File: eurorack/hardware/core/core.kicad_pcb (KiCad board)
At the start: 2 copper layers, 4 parts, among them J1 Conn, U1 STM32F427VGT6, U2 TLV320AIC23BPW, U3 LM1117F-3.3

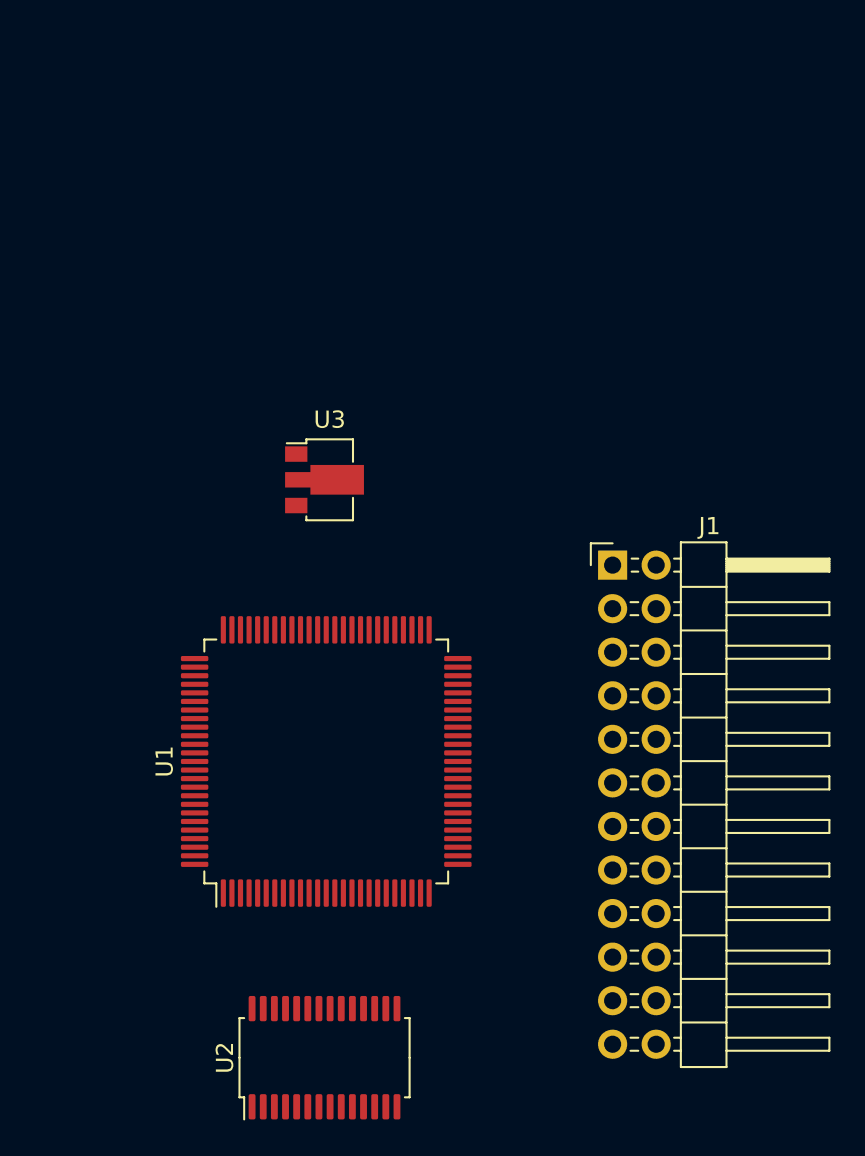
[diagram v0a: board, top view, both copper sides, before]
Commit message: Add connections to eurorack core
Signed-off-by: Petr Horacek <hrck@protonmail.com>
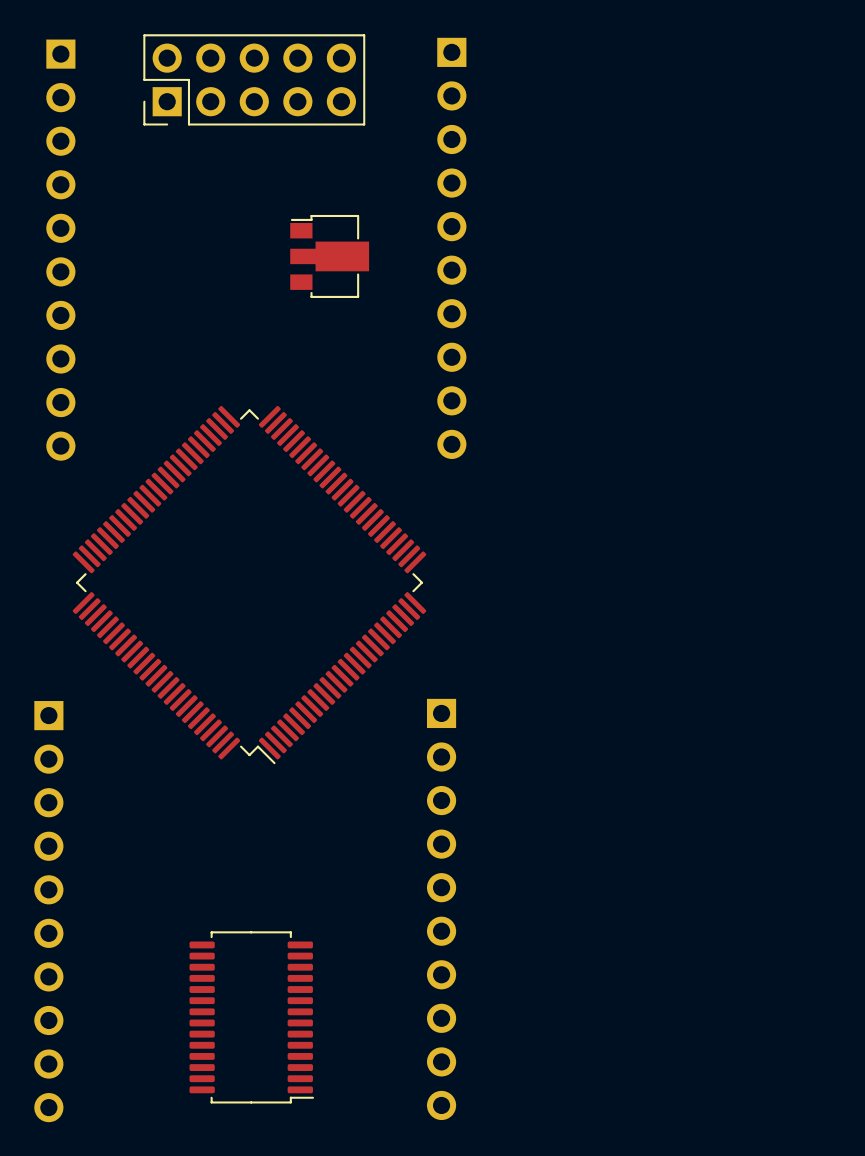
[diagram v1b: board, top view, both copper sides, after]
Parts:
- added J2: ConnSW, Connector_PinHeader_2.54mm:PinHeader_1x10_P2.54mm_Vertical, B.Cu at (111.0, 62.1)
- added J3: ConnNE, Connector_PinHeader_2.54mm:PinHeader_1x10_P2.54mm_Vertical, B.Cu at (134.4, 23.4)
- added J4: ConnSE, Connector_PinHeader_2.54mm:PinHeader_1x10_P2.54mm_Vertical, B.Cu at (133.8, 62.0)
- added J5: Power, Connector_PinHeader_2.54mm:PinHeader_2x05_P2.54mm_Vertical, F.Cu at (117.8, 26.3)
- J1: value Conn -> ConnNW; footprint Connector_PinHeader_2.54mm:PinHeader_2x12_P2.54mm_Horizontal -> Connector_PinHeader_2.54mm:PinHeader_1x10_P2.54mm_Vertical; moved to B.Cu
- moved J1 43.9 mm to (111.7, 23.6), turned to 180 degrees
- moved U3 13.0 mm to (127.3, 35.4)
- moved U1 11.3 mm to (122.7, 54.4), turned to 135 degrees
- moved U2 4.88 mm to (122.8, 79.7), turned to 180 degrees

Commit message: Add basic MCU peripherals and power
Signed-off-by: Petr Horacek <hrck@protonmail.com>
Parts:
- added C1: 20p, Capacitor_SMD:C_0402_1005Metric, F.Cu at (130.2, 65.0)
- added C2: 20p, Capacitor_SMD:C_0402_1005Metric, F.Cu at (129.5, 63.5)
- added C3: 2u2, Capacitor_SMD:C_0603_1608Metric, F.Cu at (127.9, 42.0)
- added C4: 2u2, Capacitor_SMD:C_0603_1608Metric, F.Cu at (127.9, 44.5)
- added J6: SWD, Connector_PinHeader_2.54mm:PinHeader_2x05_P2.54mm_Vertical, F.Cu at (117.8, 84.5)
- added R1: 47, Resistor_SMD:R_0402_1005Metric, F.Cu at (129.0, 65.0)
- added Y1: Crystal, Crystal:Crystal_SMD_5032-2Pin_5.0x3.2mm, F.Cu at (127.1, 68.3)
- moved U2 8.38 mm to (118.2, 72.7)
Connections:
- U1 pad 10: Net-(U1-Pad10) -> GND
- U1 pad 100: Net-(U1-Pad100) -> +3V3
- U1 pad 11: Net-(U1-Pad11) -> +3V3
- U1 pad 12: Net-(U1-Pad12) -> HSE_IN
- U1 pad 13: Net-(U1-Pad13) -> HSE_OUT
- U1 pad 19: Net-(U1-Pad19) -> +3V3
- U1 pad 20: Net-(U1-Pad20) -> GND
- U1 pad 21: Net-(U1-Pad21) -> +3.3VA
- U1 pad 22: Net-(U1-Pad22) -> +3.3VA
- U1 pad 27: Net-(U1-Pad27) -> GND
- U1 pad 28: Net-(U1-Pad28) -> +3V3
- U1 pad 50: Net-(U1-Pad50) -> +3V3
- U1 pad 6: Net-(U1-Pad6) -> +3V3
- U1 pad 74: Net-(U1-Pad74) -> GND
- U1 pad 75: Net-(U1-Pad75) -> +3V3
- U1 pad 99: Net-(U1-Pad99) -> GND

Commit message: Add reset and boot buttons
Signed-off-by: Petr Horacek <hrck@protonmail.com>
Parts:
- added R2: 10k, Resistor_SMD:R_0402_1005Metric, F.Cu at (121.6, 30.7)
- added R3: 10k, Resistor_SMD:R_0402_1005Metric, F.Cu at (124.5, 30.7)
- added SW1: Reset, Button_Switch_SMD:SW_Push_SPST_NO_Alps_SKRK, F.Cu at (130.0, 34.6)
- added SW2: Boot0, Button_Switch_SMD:SW_Push_SPST_NO_Alps_SKRK, F.Cu at (117.0, 34.5)
- moved U3 4.17 mm to (123.2, 36.2)
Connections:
- U1 pad 14: Net-(U1-Pad14) -> NRST
- U1 pad 94: Net-(U1-Pad94) -> BOOT0

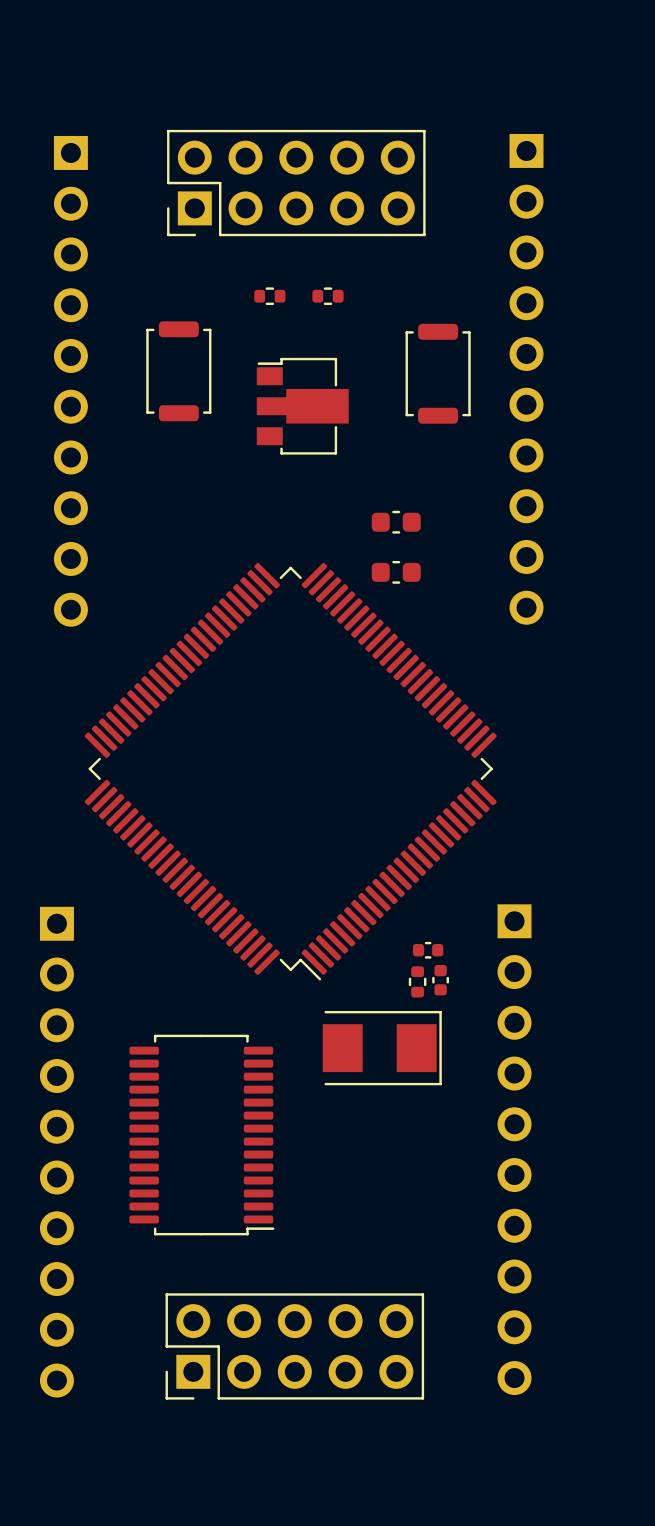
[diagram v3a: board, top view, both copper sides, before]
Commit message: Isoolate 3.3v power from MCU
Signed-off-by: Petr Horacek <hrck@protonmail.com>
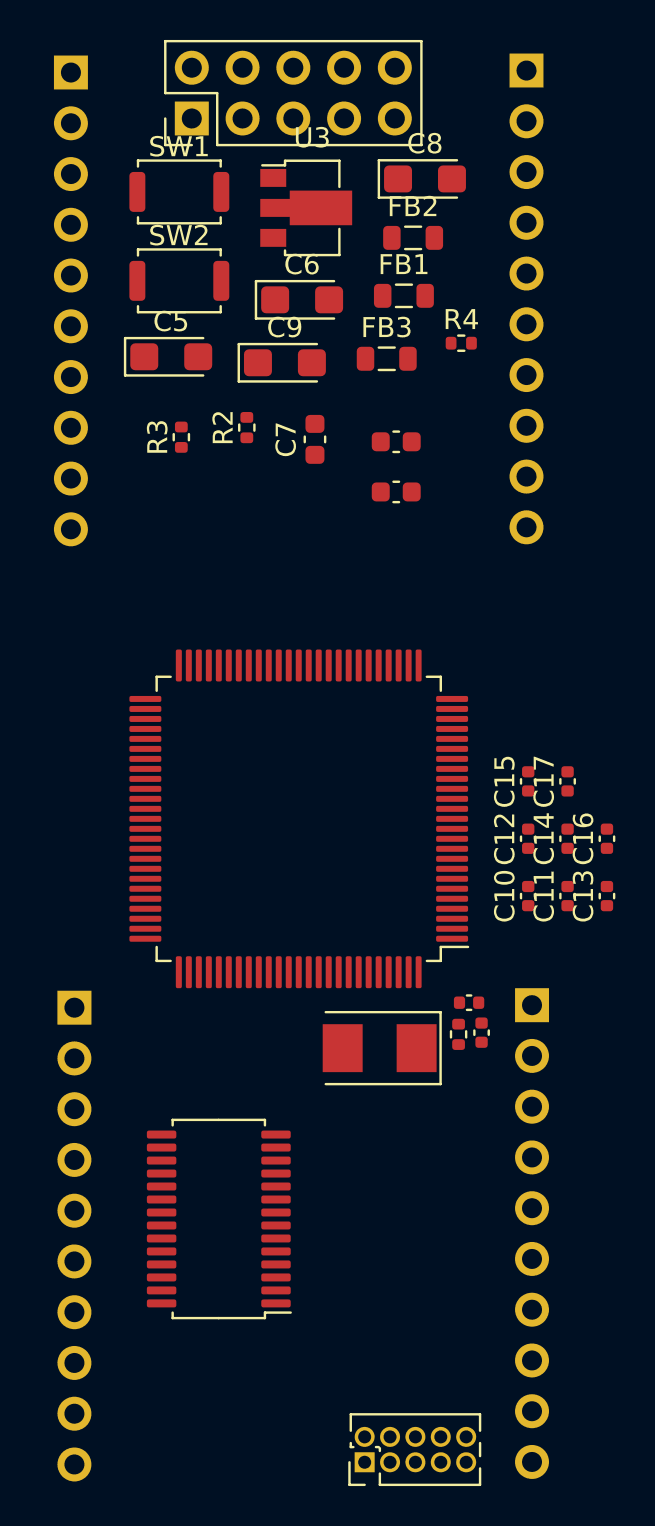
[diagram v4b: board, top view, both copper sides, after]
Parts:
- added C10: 1u, Capacitor_SMD:C_0402_1005Metric, F.Cu at (134.5, 60.7)
- added C11: 100n, Capacitor_SMD:C_0402_1005Metric, F.Cu at (136.5, 60.7)
- added C12: 100n, Capacitor_SMD:C_0402_1005Metric, F.Cu at (134.5, 57.9)
- added C13: 100n, Capacitor_SMD:C_0402_1005Metric, F.Cu at (138.5, 60.7)
- added C14: 100n, Capacitor_SMD:C_0402_1005Metric, F.Cu at (136.5, 57.9)
- added C15: 100n, Capacitor_SMD:C_0402_1005Metric, F.Cu at (134.5, 55.0)
- added C16: 100n, Capacitor_SMD:C_0402_1005Metric, F.Cu at (138.5, 57.9)
- added C17: 100n, Capacitor_SMD:C_0402_1005Metric, F.Cu at (136.5, 55.0)
- added C5: 47u, Capacitor_Tantalum_SMD:CP_EIA-3216-18_Kemet-A, F.Cu at (116.7, 33.8)
- added C6: 47u, Capacitor_Tantalum_SMD:CP_EIA-3216-18_Kemet-A, F.Cu at (123.2, 30.9)
- added C7: 2u2, Capacitor_SMD:C_0603_1608Metric, F.Cu at (123.9, 37.9)
- added C8: 47u, Capacitor_Tantalum_SMD:CP_EIA-3216-18_Kemet-A, F.Cu at (129.4, 24.9)
- added C9: 47u, Capacitor_Tantalum_SMD:CP_EIA-3216-18_Kemet-A, F.Cu at (122.4, 34.1)
- added FB1: Ferrite_Bead_Small, Inductor_SMD:L_0805_2012Metric, F.Cu at (128.3, 30.7)
- added FB2: Ferrite_Bead_Small, Inductor_SMD:L_0805_2012Metric, F.Cu at (128.8, 27.8)
- added FB3: Ferrite_Bead_Small, Inductor_SMD:L_0805_2012Metric, F.Cu at (127.5, 33.9)
- added R4: 15, Resistor_SMD:R_0402_1005Metric, F.Cu at (131.2, 33.1)
- J6: footprint Connector_PinHeader_2.54mm:PinHeader_2x05_P2.54mm_Vertical -> Connector_PinHeader_1.27mm:PinHeader_2x05_P1.27mm_Vertical
- moved SW1 15.8 mm to (117.1, 25.5), turned to 0 degrees
- moved R3 10.2 mm to (117.2, 37.8), turned to 90 degrees
- moved U3 9.93 mm to (123.4, 26.3)
- moved J6 9.70 mm to (126.3, 89.1)
- moved R2 6.67 mm to (120.5, 37.3), turned to 90 degrees
- moved SW2 4.53 mm to (117.1, 30.0), turned to 0 degrees
- moved J5 4.50 mm to (117.7, 21.8)
- moved J2 4.29 mm to (111.8, 66.3)
- moved J4 4.29 mm to (134.7, 66.2)
- moved U2 4.29 mm to (119.0, 76.9)
- moved J1 4.03 mm to (111.7, 19.5)
- moved C3 4.02 mm to (127.9, 38.0)
- moved C4 4.02 mm to (127.9, 40.5)
- moved J3 4.02 mm to (134.4, 19.4)
- moved R1 3.33 mm to (131.1, 67.7)
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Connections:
- J5 pad 1: Net-(J5-Pad1) -> Net-(FB1-Pad1)
- J5 pad 10: Net-(J5-Pad10) -> Net-(FB2-Pad1)
- J5 pad 2: Net-(J5-Pad2) -> Net-(FB1-Pad1)
- J5 pad 3: Net-(J5-Pad3) -> GND
- J5 pad 4: Net-(J5-Pad4) -> GND
- J5 pad 5: Net-(J5-Pad5) -> GND
- J5 pad 6: Net-(J5-Pad6) -> GND
- J5 pad 7: Net-(J5-Pad7) -> GND
- J5 pad 8: Net-(J5-Pad8) -> GND
- J5 pad 9: Net-(J5-Pad9) -> Net-(FB2-Pad1)
- U3 pad 1: Net-(U3-Pad1) -> GND
- U3 pad 2: Net-(U3-Pad2) -> +3V3

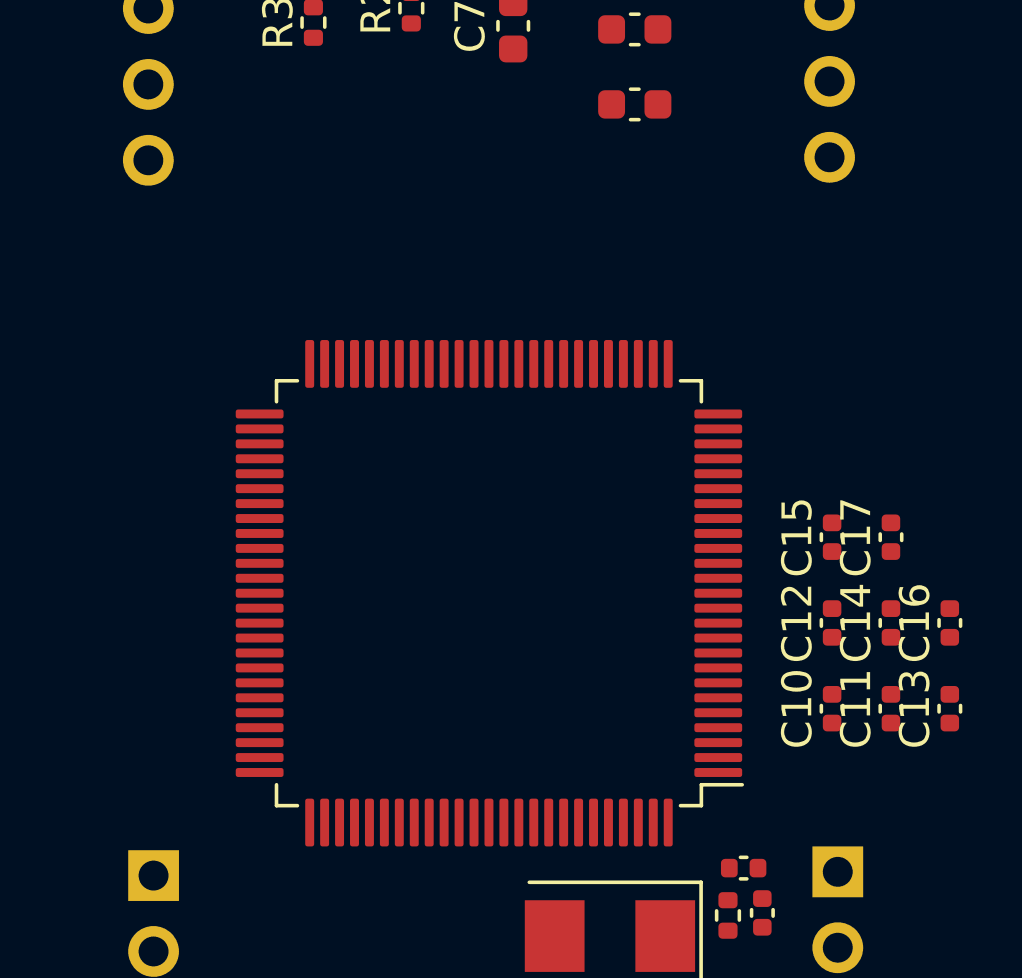
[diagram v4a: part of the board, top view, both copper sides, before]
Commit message: Add decoupling capacitors
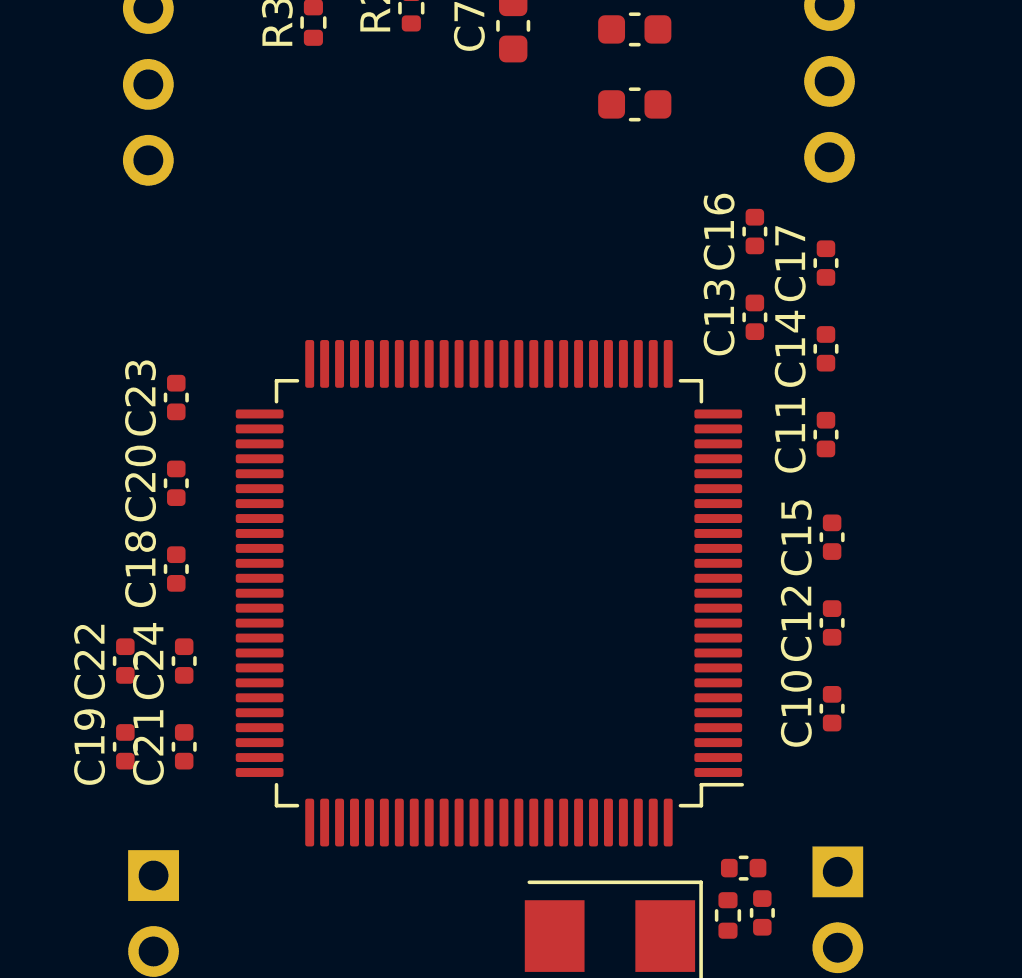
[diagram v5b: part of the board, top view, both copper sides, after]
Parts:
- added C18: 100n, Capacitor_SMD:C_0402_1005Metric, F.Cu at (112.6, 56.1)
- added C19: 100n, Capacitor_SMD:C_0402_1005Metric, F.Cu at (110.9, 62.0)
- added C20: 1u, Capacitor_SMD:C_0402_1005Metric, F.Cu at (112.6, 53.2)
- added C21: 100n, Capacitor_SMD:C_0402_1005Metric, F.Cu at (112.9, 62.0)
- added C22: 100n, Capacitor_SMD:C_0402_1005Metric, F.Cu at (110.9, 59.1)
- added C23: 100n, Capacitor_SMD:C_0402_1005Metric, F.Cu at (112.6, 50.3)
- added C24: 100n, Capacitor_SMD:C_0402_1005Metric, F.Cu at (112.9, 59.1)
- moved C16 14.6 mm to (132.0, 44.8)
- moved C13 14.6 mm to (132.0, 47.6)
- moved C17 9.43 mm to (134.3, 45.8)
- moved C11 9.43 mm to (134.3, 51.6)
- moved C14 9.43 mm to (134.3, 48.7)
